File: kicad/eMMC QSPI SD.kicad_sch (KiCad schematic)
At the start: 23 parts, among them J1 GT-TF003-H0185-01, U10 THGBMNG5D1LBAIL, U11 ZD25WQ80BOIGT, U12 IP4252CZ16-8-TTL

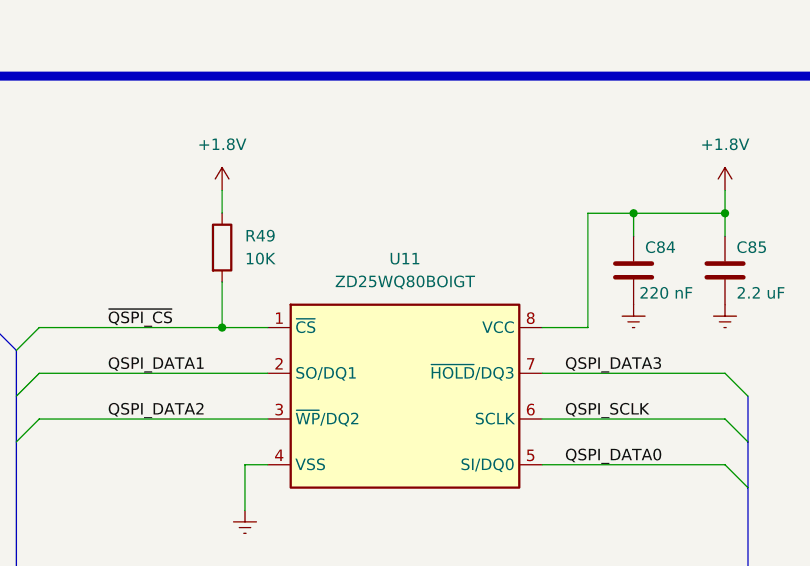
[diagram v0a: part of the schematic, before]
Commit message: Change schematic and PCB
  changed component U11 from 8MBit to 32 MBit
  added qr-code on bottom overlay
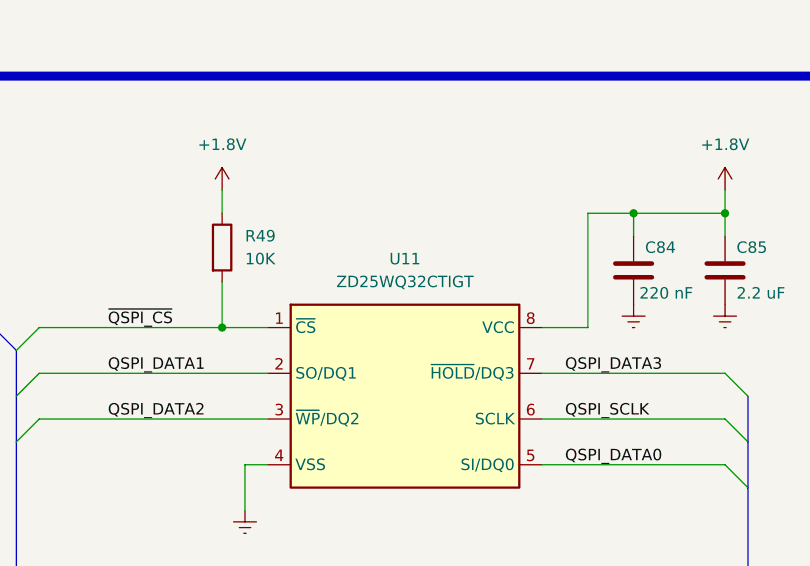
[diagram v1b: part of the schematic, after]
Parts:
- removed U11: ZD25WQ80BOIGT, Package_SO:TSSOP-8_4.4x3mm_P0.65mm, symbol -- database:Integrated/INT-ZD25WQ80BOIGT
- added U11: ZD25WQ32CTIGT, Package_SO:SOP-8_3.9x4.9mm_P1.27mm, symbol db:Integrated/INT-ZD25WQ32CTIGT
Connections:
- net +1.8V: now also U11.8 (VCC)
- net GNDREF: now also U11.4 (VSS)
- net QSPI_DATA0: now also U11.5 (SI/DQ0)
- net QSPI_DATA1: now also U11.2 (SO/DQ1)
- net QSPI_DATA2: now also U11.3 (~{WP}/DQ2)
- net QSPI_DATA3: now also U11.7 (~{HOLD}/DQ3)
- net QSPI_SCLK: now also U11.6 (SCLK)
- net ~{QSPI_CS}: now also U11.1 (~{CS})
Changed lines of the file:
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@@
+	)
+	(symbol
+		(lib_id "db:Integrated/INT-ZD25WQ32CTIGT")
+		(at 289.56 76.2 0)
+		(unit 1)
+		(exclude_from_sim no)
+		(in_bom yes)
+		(on_board yes)
+		(dnp no)
+		(fields_autoplaced yes)
+		(property "Reference" "U11"
+			(at 302.26 71.12 0)
+			(effects
+				(font
+					(size 1.27 1.27)
+				)
+			)
+		)
+		(property "Value" "ZD25WQ32CTIGT"
+			(at 302.26 73.66 0)
+			(effects
+				(font
+					(size 1.27 1.27)
+				)
+			)
+		)
+		(property "Footprint" "Package_SO:SOP-8_3.9x4.9mm_P1.27mm"
+			(at 289.56 76.2 0)
+			(effects
+				(font
+					(size 1.27 1.27)
+				)
+				(hide yes)
+			)
+		)
+		(property "Datasheet" "https://wmsc.lcsc.com/wmsc/upload/file/pdf/v2/lcsc/2211290930_Zetta-ZD25WQ32CTIGT_C5290169.pdf"
+			(at 289.56 76.2 0)
+			(effects
+				(font
+					(size 1.27 1.27)
+				)
+				(hide yes)
+			)
+		)
+		(property "Description" "SOP8 - 32Mbit QSPI 104MHz NOR FLASH"
+			(at 289.56 76.2 0)
+			(effects
+				(font
+					(size 1.27 1.27)
+				)
+				(hide yes)
+			)
+		)
+		(property "Manufacturer" "Zetta"
+			(at 289.56 76.2 0)
+			(effects
+				(font
+					(size 1.27 1.27)
+				)
+				(hide yes)
+			)
+		)
+		(property "MPN" "ZD25WQ32CTIGT"
+			(at 289.56 76.2 0)
+			(show_name yes)
+			(effects
+				(font
+					(size 1.27 1.27)
+				)
+				(hide yes)
+			)
+		)
+		(property "LCSC" "C5290169"
+			(at 289.56 76.2 0)
+			(show_name yes)
+			(effects
+				(font
+					(size 1.27 1.27)
+				)
+				(hide yes)
+			)
+		)
+		(property "Stock" "0"
+			(at 289.56 76.2 0)
+			(show_name yes)
+			(effects
+				(font
+					(size 1.27 1.27)
+				)
+				(hide yes)
+			)
+		)
+		(pin "2"
+		)
+		(pin "1"
+		)
+		(pin "5"
+		)
+		(pin "3"
+		)
+		(pin "8"
+		)
+		(pin "6"
+		)
+		(pin "4"
+		)
+		(pin "7"
+		)
+		(instances
+			(project ""
+				(path "/22d28cd1-1a5f-4d07-89a7-8fe714f4fb3d/eb948cab-b149-4301-ad44-286ab772f156/a6b73352-4156-4230-8828-44cad06e0e52"
+					(reference "U11")
+					(unit 1)
+				)
+			)
+		)
 	)
 	(symbol
@@
 					(unit 1)
 				)
-			)
-		)
-	)
-	(symbol
-		(lib_id "-- database:Integrated/INT-ZD25WQ80BOIGT")
-		(at 289.56 76.2 0)
-		(unit 1)
-		(exclude_from_sim no)
-		(in_bom yes)
-		(on_board yes)
-		(dnp no)
-		(fields_autoplaced yes)
-		(property "Reference" "U11"
-			(at 302.26 71.12 0)
-			(effects
-				(font
-					(size 1.27 1.27)
-				)
-			)
-		)
-		(property "Value" "ZD25WQ80BOIGT"
-			(at 302.26 73.66 0)
-			(effects
-				(font
-					(size 1.27 1.27)
-				)
-			)
-		)
-		(property "Footprint" "Package_SO:TSSOP-8_4.4x3mm_P0.65mm"
-			(at 289.56 76.2 0)
-			(effects
-				(font
-					(size 1.27 1.27)
-				)
-				(hide yes)
-			)
-		)
-		(property "Datasheet" "https://wmsc.lcsc.com/wmsc/upload/file/pdf/v2/lcsc/2108150430_Zetta-ZD25WQ80BOIGT_C2875857.pdf"
-			(at 289.56 76.2 0)
-			(effects
-				(font
-					(size 1.27 1.27)
-				)
-				(hide yes)
-			)
-		)
-		(property "Description" "TSSOP8 - 8Mbit QSPI TSSOP8 NOR FLASH"
-			(at 289.56 76.2 0)
-			(effects
-				(font
-					(size 1.27 1.27)
-				)
-				(hide yes)
-			)
-		)
-		(property "LCSC" "C2875857"
-			(at 289.56 76.2 0)
-			(effects
-				(font
-					(size 1.27 1.27)
-				)
-				(hide yes)
-			)
-		)
-		(property "Manufacturer" "Zetta"
-			(at 289.56 76.2 0)
-			(effects
-				(font
-					(size 1.27 1.27)
-				)
-				(hide yes)
-			)
-		)
-		(property "MPN" "ZD25WQ80BOIGT"
-			(at 289.56 76.2 0)
-			(show_name yes)
-			(effects
-				(font
-					(size 1.27 1.27)
-				)
-				(hide yes)
-			)
-		)
-		(property "Stock" "0"
-			(at 289.56 76.2 0)
-			(show_name yes)
-			(effects
-				(font
-					(size 1.27 1.27)
-				)
-				(hide yes)
-			)
-		)
-		(pin "2"
-		)
-		(pin "8"
-		)
-		(pin "4"
-		)
-		(pin "3"
-		)
-		(pin "1"
-		)
-		(pin "5"
-		)
-		(pin "6"
-		)
-		(pin "7"
-		)
-		(instances
-			(project "iMX6 Demo Board"
-				(path "/22d28cd1-1a5f-4d07-89a7-8fe714f4fb3d/eb948cab-b149-4301-ad44-286ab772f156/a6b73352-4156-4230-8828-44cad06e0e52"
-					(reference "U11")
-					(unit 1)
-				)

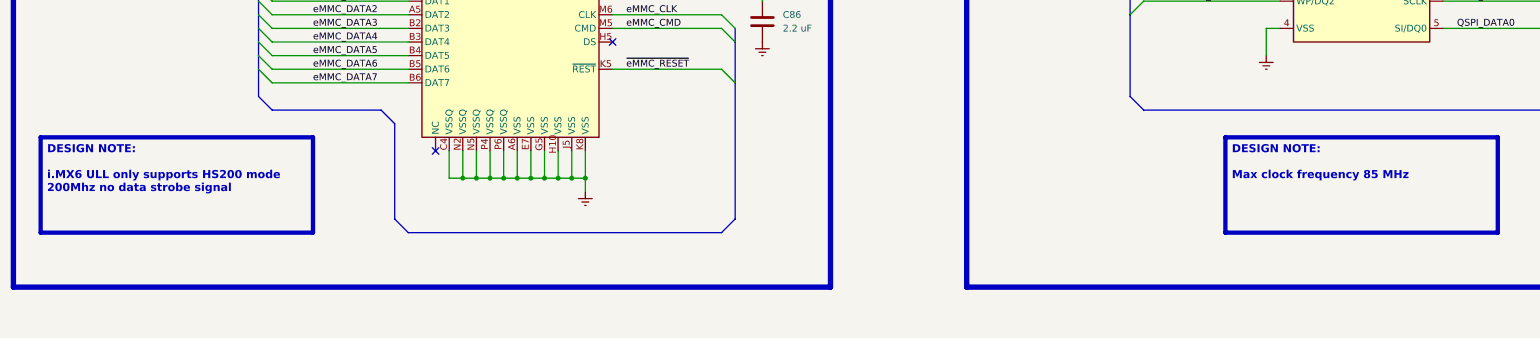
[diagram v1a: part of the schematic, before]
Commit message: Fix hardware bugs - Fix part number in bom for resistors R103, R113, R114, R118 -> 680K - Fix part number in BOM for resistors R13, R16 -> 68K - Fix part number in BOM for resistor R14 -> 4.7K - Fix part number in BOM for capacitors C100, C101, C12, C13, C130, C131, C133, C135, C140, C141, C15, C19, C57, C58, C7, C99 -> 100nF - Fix footprint for USB-A connectors - Fix power buttom pull-up resistor connection -> connect to +3.3V_STAND_BY
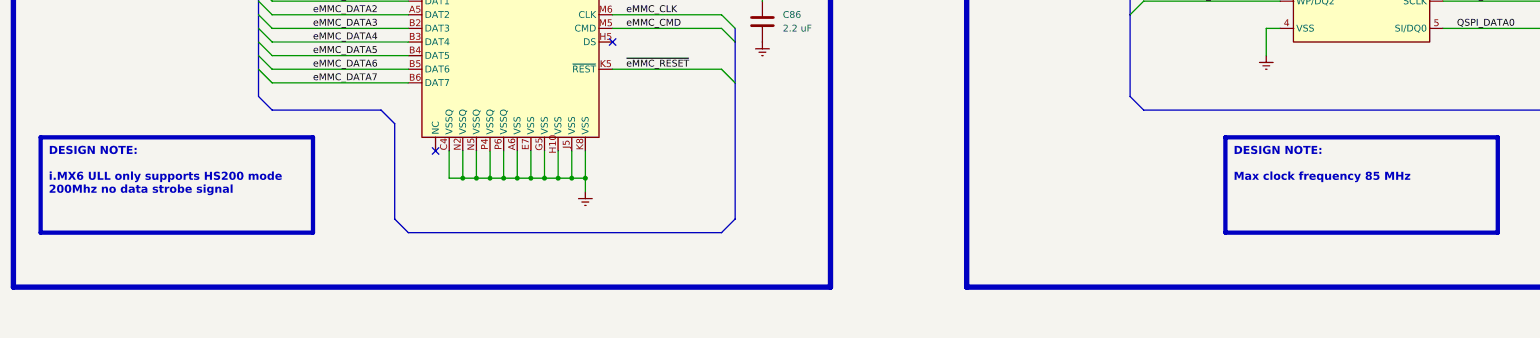
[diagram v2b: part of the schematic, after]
